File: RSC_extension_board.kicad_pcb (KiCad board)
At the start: 2 copper layers, 21 parts, among them J1 Conn_01x03, J2 Conn_01x03, J3 Conn_01x03, J4 Raspberry_Pi_4, J5 Conn_01x04, J6 USB_C_Receptacle_PowerOnly_6P, J7 Conn_01x02, Q1 BSS138

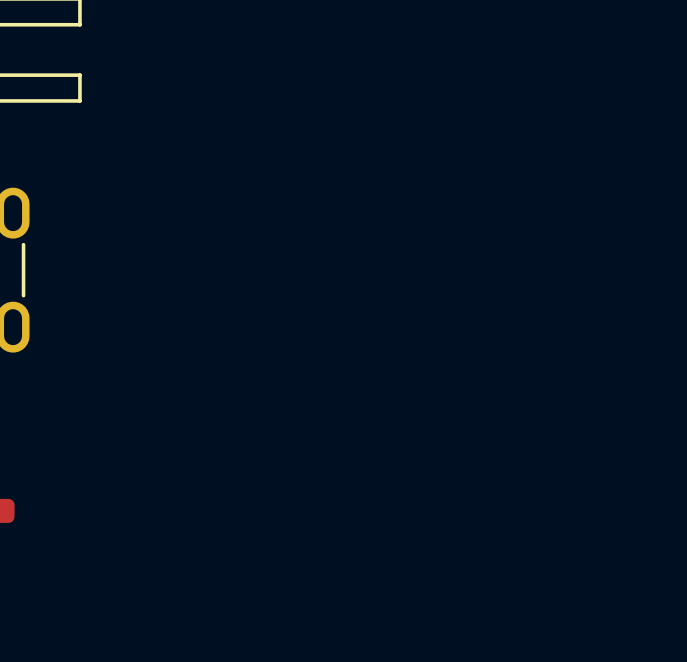
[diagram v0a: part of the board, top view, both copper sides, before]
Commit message: added some tvs diodes. symbols weird
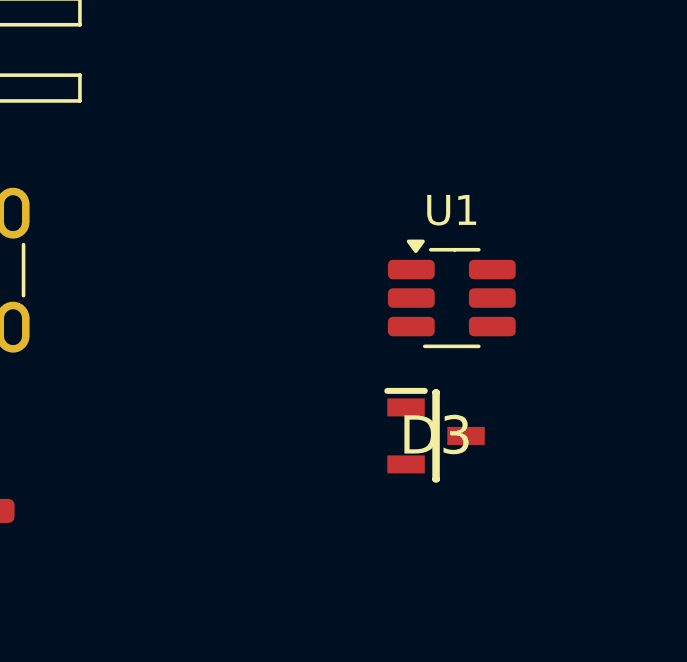
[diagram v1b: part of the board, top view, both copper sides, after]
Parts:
- added D3: CDSOT23-T05, CDSOT23-T05:SOT95P230X117-3N, F.Cu at (143.5, 76.5)
- added U1: USBLC6-2SC6, Package_TO_SOT_SMD:SOT-23-6_Handsoldering, F.Cu at (144.0, 71.9)
- R3, R4: value R -> 5.1k
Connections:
- J6 pad A5: unconnected-(J6-CC1-PadA5) -> Net-(J6-CC1)
- J6 pad B5: unconnected-(J6-CC2-PadB5) -> Net-(J6-CC2)
- R3 pad 1: unconnected-(R3-Pad1) -> Net-(J6-CC2)
- R3 pad 2: unconnected-(R3-Pad2) -> Earth
- R4 pad 1: unconnected-(R4-Pad1) -> Net-(J6-CC1)
- R4 pad 2: unconnected-(R4-Pad2) -> Earth

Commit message: bit of power circuit
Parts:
- added C5: 100nF, Capacitor_SMD:C_0603_1608Metric_Pad1.08x0.95mm_HandSolder, F.Cu at (143.3, 77.9)
- added F1: SMDC300F_24-2, SMDC300F_24-2:SMDC030F2, F.Cu at (147.0, 68.4)
- added SW1: SW_Wuerth_450301014042, Button_Switch_THT:SW_Slide-03_Wuerth-WS-SLTV_10x2.5x6.4_P2.54mm, F.Cu at (146.9, 74.6)
- moved D3 8.07 mm to (136.0, 73.6)
- moved U1 8.07 mm to (136.5, 69.0)
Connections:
- D3 pad 1: unconnected-(D3-ANODE_1-Pad1) -> Earth
- D3 pad 2: unconnected-(D3-ANODE_2-Pad2) -> Earth
- D3 pad 3: unconnected-(D3-CATHODE-Pad3) -> Net-(U1-VBUS)
- J6 pad A9: +5V -> Net-(U1-VBUS)
- J6 pad B9: +5V -> Net-(U1-VBUS)
- R3 pad 1: Net-(J6-CC2) -> Net-(R3-Pad1)
- R4 pad 1: Net-(J6-CC1) -> Net-(R4-Pad1)
- U1 pad 1: unconnected-(U1-I/O1-Pad1) -> Net-(J6-CC1)
- U1 pad 2: unconnected-(U1-GND-Pad2) -> Earth
- U1 pad 3: unconnected-(U1-I/O2-Pad3) -> Net-(J6-CC2)
- U1 pad 4: unconnected-(U1-I/O2-Pad4) -> Net-(R3-Pad1)
- U1 pad 5: unconnected-(U1-VBUS-Pad5) -> Net-(U1-VBUS)
- U1 pad 6: unconnected-(U1-I/O1-Pad6) -> Net-(R4-Pad1)

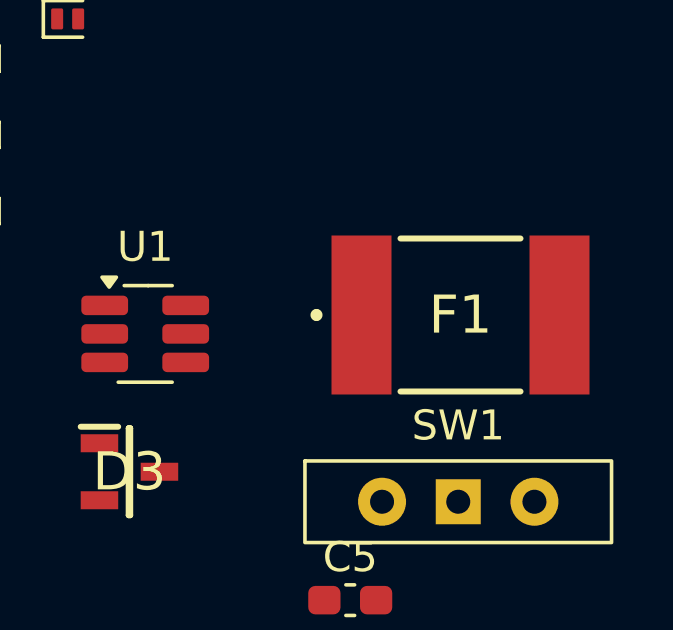
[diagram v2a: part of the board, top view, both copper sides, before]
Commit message: updated fuse
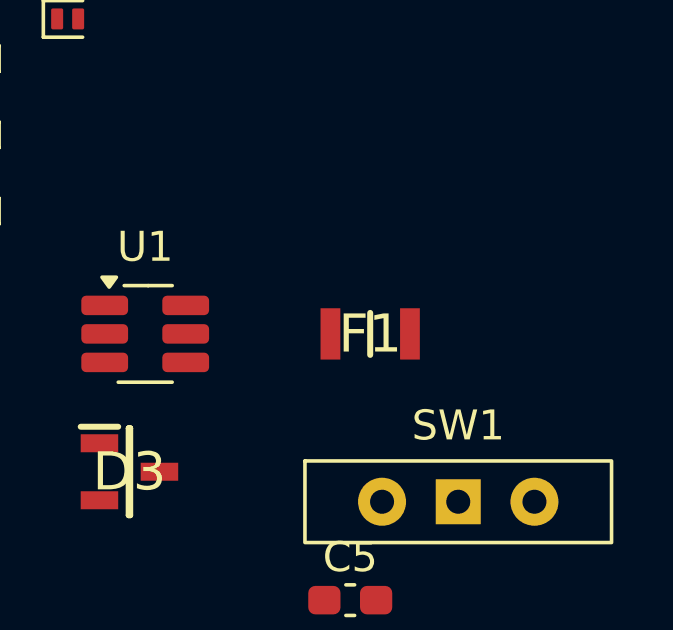
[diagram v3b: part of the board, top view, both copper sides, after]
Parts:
- F1: value SMDC300F_24-2 -> PTSLR08058V350; footprint SMDC300F_24-2:SMDC030F2 -> PTSLR08058V350:FUSC2516X100N
- moved F1 3.08 mm to (144.0, 69.0)

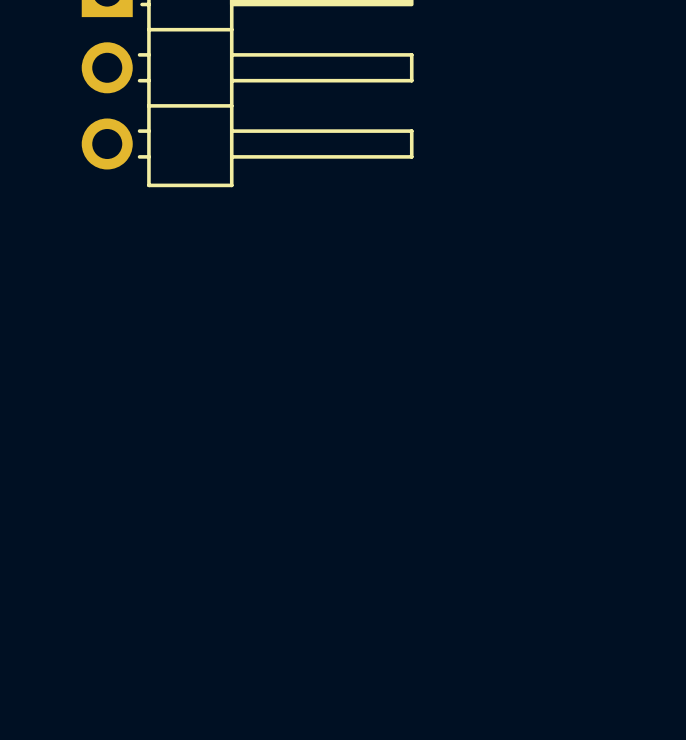
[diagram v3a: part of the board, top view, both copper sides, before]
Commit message: qwiic connector and 3.3v led out
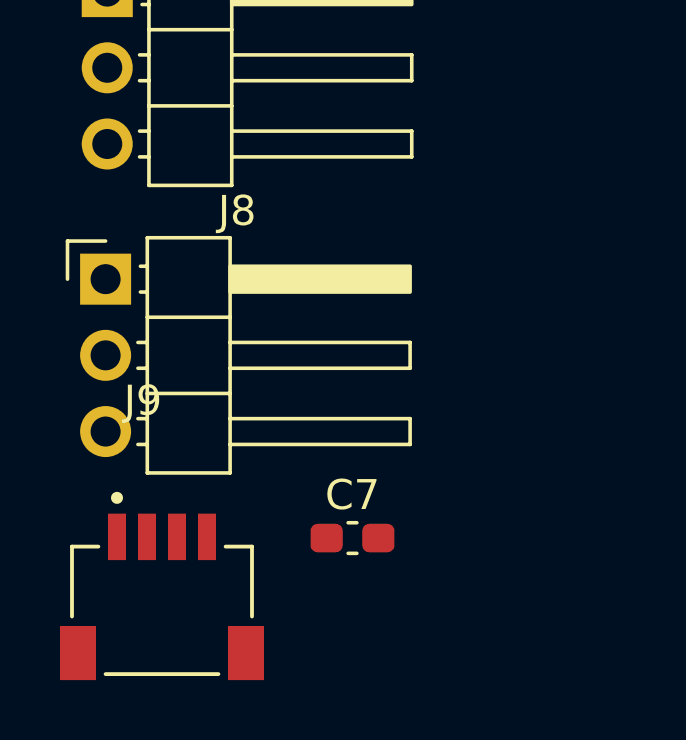
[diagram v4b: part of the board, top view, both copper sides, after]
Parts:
- added C7: 100nF, Capacitor_SMD:C_0603_1608Metric_Pad1.08x0.95mm_HandSolder, F.Cu at (107.6, 94.8)
- added J8: Conn_01x03, Connector_PinHeader_2.54mm:PinHeader_1x03_P2.54mm_Horizontal, F.Cu at (99.4, 86.2)
- added J9: PRT-14417, PRT-14417:SPARKFUN_PRT-14417, F.Cu at (101.2, 97.2)
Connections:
- J4 pad 3: unconnected-(J4-SDA_I2C1/GPIO02-Pad3) -> /SDA
- J4 pad 5: unconnected-(J4-SCL_I2C1/GPIO03-Pad5) -> /SCL

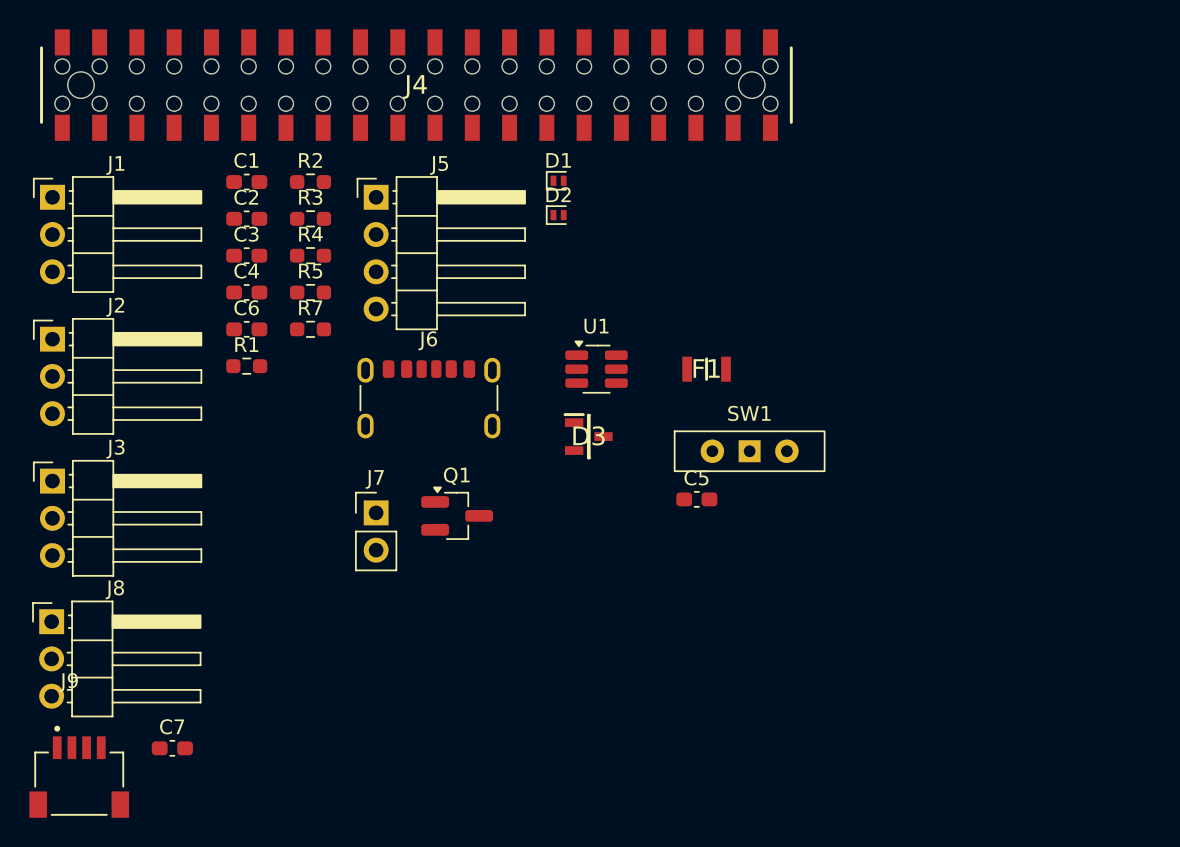
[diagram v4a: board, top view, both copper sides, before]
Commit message: new tvs diodes
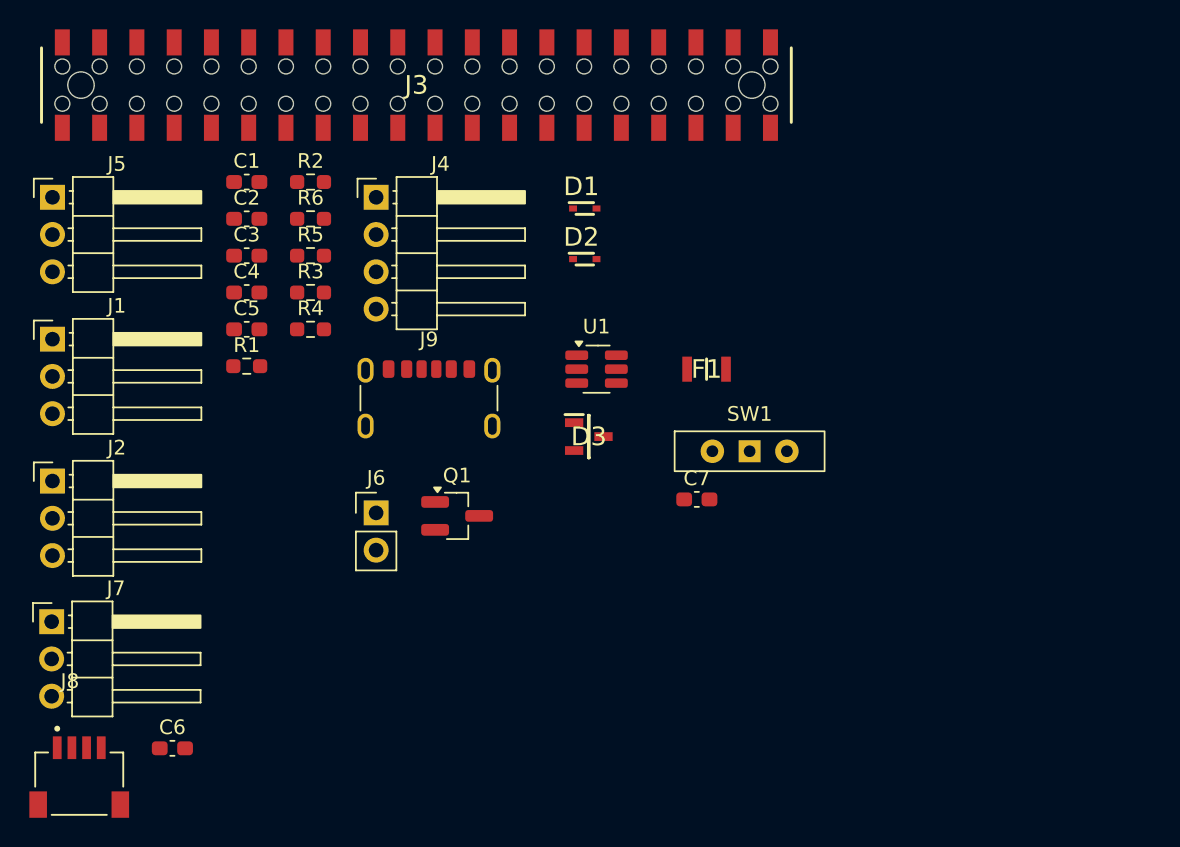
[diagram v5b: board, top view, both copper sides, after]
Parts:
- D1, D2: value PESD3V3S1UL -> PJSD03TS-AU_R1_000A1; footprint Diode_SMD:D_SOD-882 -> PJSD03TS-AU_R1_000A1:SODFL1608X65N
- moved D2 3.49 mm to (135.7, 61.5)
- moved D1 2.60 mm to (135.7, 58.0)
- renumbered C6 to C5, C7 to C6, C5 to C7, J2 to J1, J3 to J2, J4 to J3, J5 to J4, J1 to J5, J7 to J6, J8 to J7, J9 to J8, J6 to J9, R5 to R3, R7 to R4, R4 to R5, R3 to R6

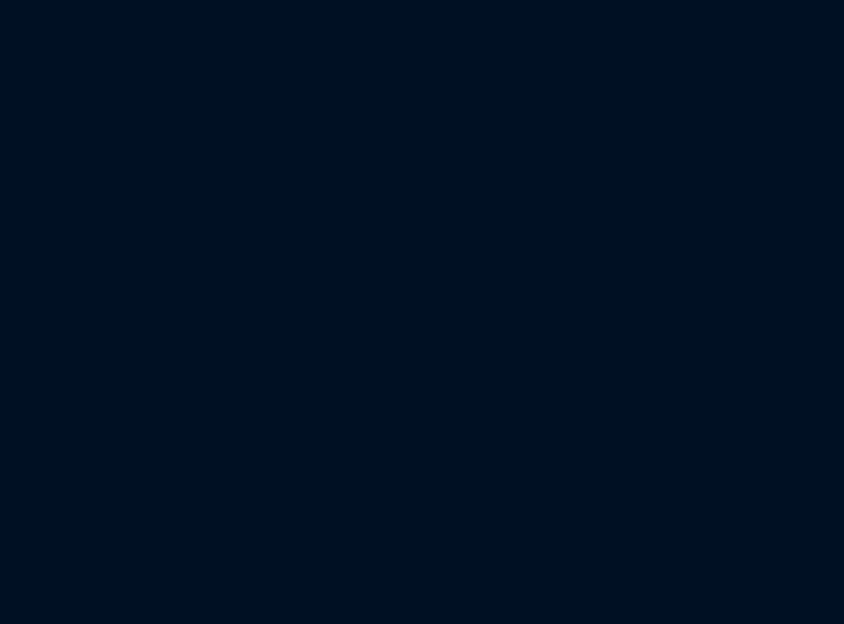
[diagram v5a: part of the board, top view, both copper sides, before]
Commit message: added possibility for button led dimming
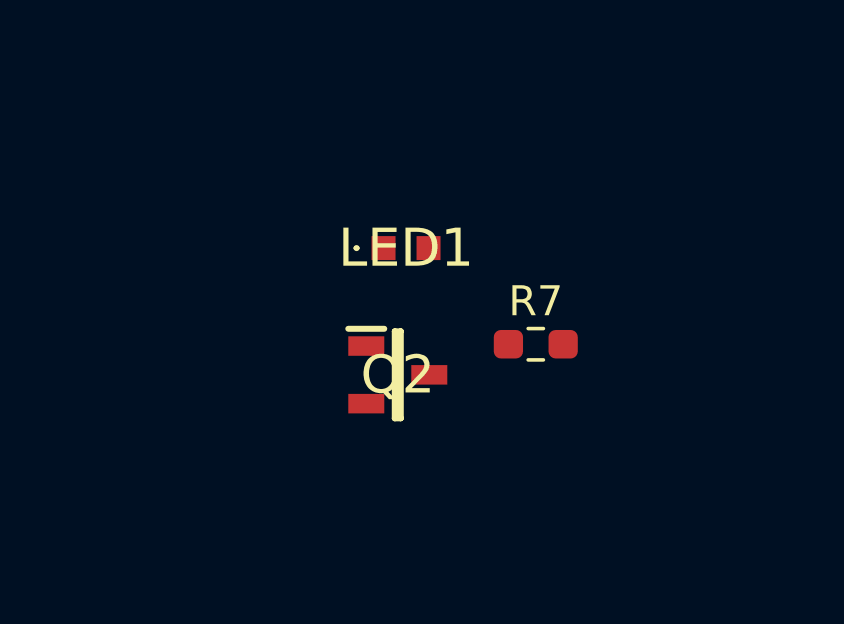
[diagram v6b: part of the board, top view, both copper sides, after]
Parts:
- added LED1: KR_EELP41.22-Q1S1-36-A8J8-020-R18, KR_EELP41.22-Q1S1-36-A8J8-020-R18:KREELP4122Q1S136A8J8020R18, F.Cu at (139.5, 89.0)
- added Q2: 2N7002-7-F, 2N7002-7-F:SOT96P240X120-3N, F.Cu at (139.2, 93.3)
- added R7: 150, Resistor_SMD:R_0603_1608Metric_Pad0.98x0.95mm_HandSolder, F.Cu at (143.8, 92.2)

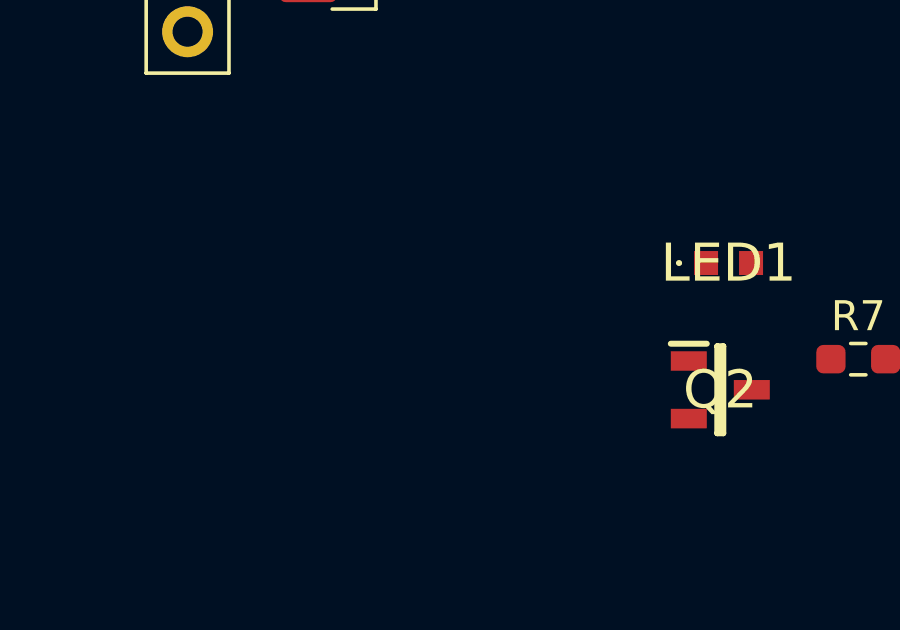
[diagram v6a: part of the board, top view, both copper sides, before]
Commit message: voice schematic switch, 3d files
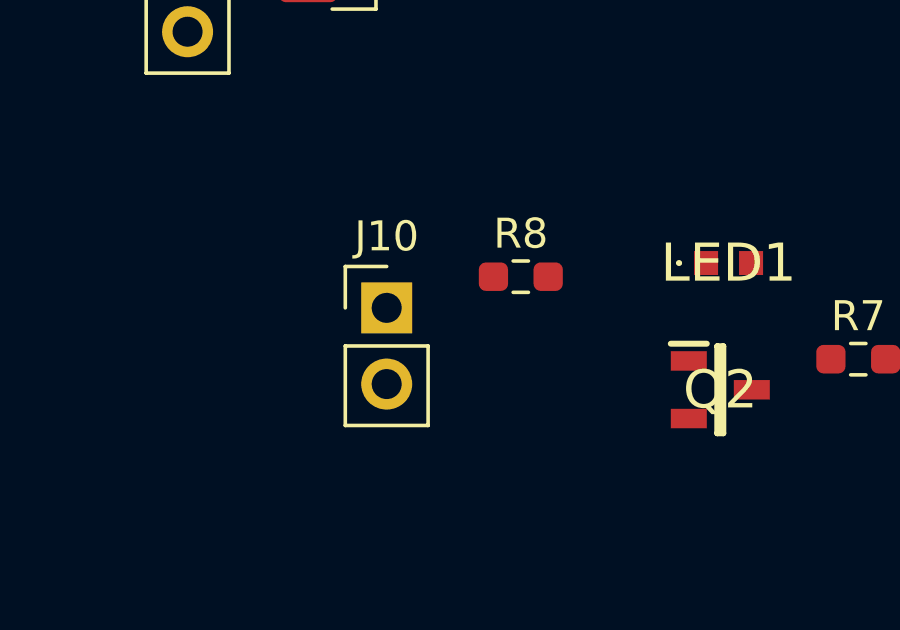
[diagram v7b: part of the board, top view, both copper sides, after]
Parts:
- added J10: Conn_01x02, Connector_PinHeader_2.54mm:PinHeader_1x02_P2.54mm_Vertical, F.Cu at (128.1, 90.5)
- added R8: 150, Resistor_SMD:R_0603_1608Metric_Pad0.98x0.95mm_HandSolder, F.Cu at (132.6, 89.5)
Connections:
- J3 pad 12: unconnected-(J3-GPIO18/SPI1_~{CE0}/PCM_CLK/PWM0-Pad12) -> /I2S_BCLK
- J3 pad 35: unconnected-(J3-GPIO19/SPI1_MISO/PCM_FS-Pad35) -> /I2S_LRCLK
- J3 pad 38: unconnected-(J3-GPIO20/SPI1_MOSI/PCM_DIN/PWM1-Pad38) -> /I2S_DIN
- J3 pad 40: unconnected-(J3-GPIO21/SPI1_SCLK/PCM_DOUT-Pad40) -> /I2S_DOUT
- Q2 pad 1: unconnected-(Q2-G-Pad1) -> Net-(Q2-G)
- Q2 pad 2: unconnected-(Q2-S-Pad2) -> Earth
- Q2 pad 3: unconnected-(Q2-D-Pad3) -> Net-(J10-Pin_1)
